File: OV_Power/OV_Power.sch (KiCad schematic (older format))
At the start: 43 parts, among them J4 SpadeLug, J5 SpadeLug, Q1 SSM3K341R, Q2 2N7002BK, U1 LT3796, U2 LT1936

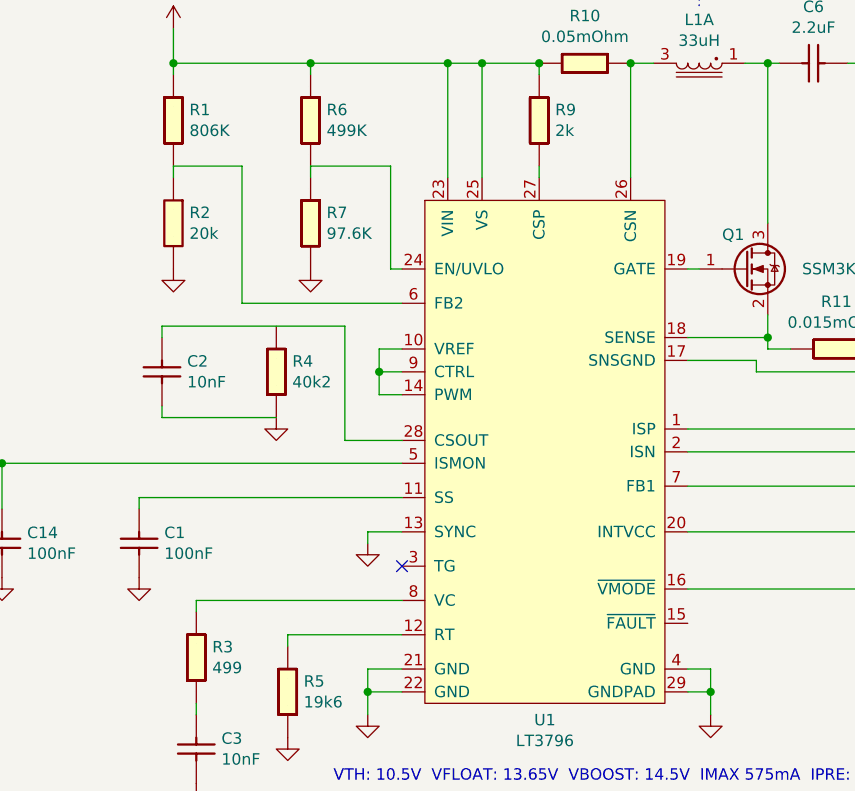
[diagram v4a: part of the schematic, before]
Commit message: Finished schemo and placement of power supply board, then resolved interconnects with the main board.
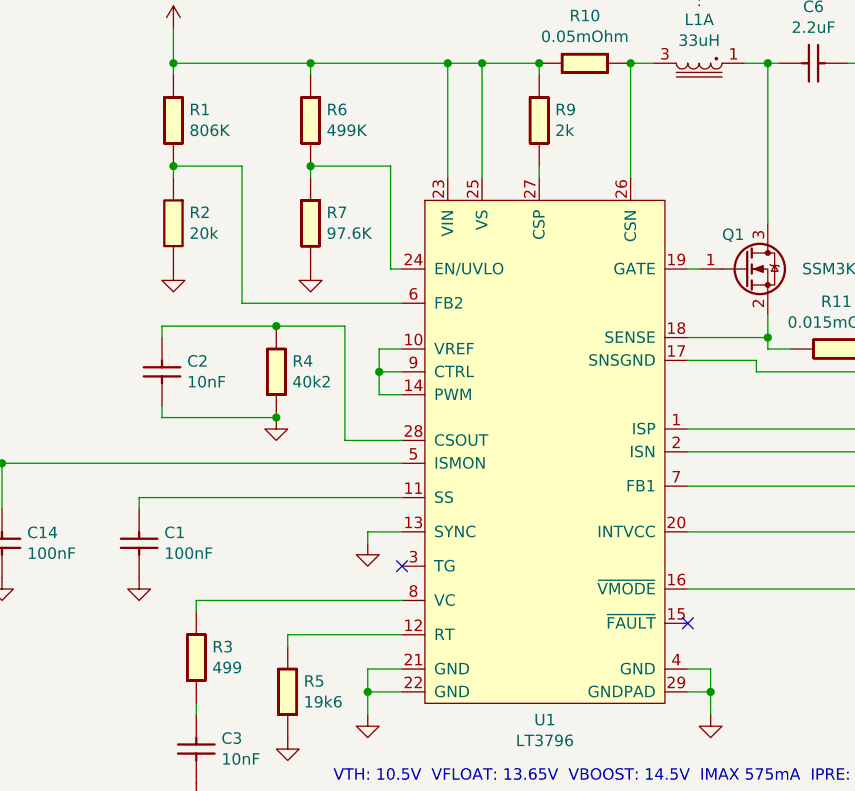
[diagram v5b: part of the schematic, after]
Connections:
- net at C2.1, U1.28 (CSOUT): now also R4.1
- no-connect marks 1 -> 2
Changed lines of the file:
@@
 NoConn ~ 4100 3250
 Wire Wire Line
-	3050 2200 3850 2200
+	3050 2200 3550 2200
 $Sheet
 S 9850 5800 1350 150
@@
 Connection ~ 4700 1050
 Connection ~ 5100 1050
+Connection ~ 3550 2200
+Wire Wire Line
+	3550 2200 3850 2200
+Connection ~ 3550 2600
+Connection ~ 3100 1500
+Connection ~ 3700 1500
+NoConn ~ 5350 3500
 $EndSCHEMATC

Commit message: First cut at complete routing for the power board.  Still need DRC checking and final fettling of the BOM and silkscreens before going to press.
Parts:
- added C15: 100nF_0603_Ceramic_Capacitor,_10%,_X7R,_25V, Capacitor_SMD:C_0603_1608Metric, symbol OpenVent:100nF_0603_Ceramic_Capacitor,_10%,_X7R,_25V
- C5: Tolerance (none) -> 10%; Voltage (none) -> 25V
- D2: Voltage (none) -> 100V
- J4: symbol OV_Power-rescue:SpadeLug-F_connectors -> F_connectors:SpadeLug; Mfr_PN (none) -> 1217861-1
- J5: Mfr_PN (none) -> 1217861-1
- R10, R11, R12, R15: Tolerance (none) -> 1%
- RT1: Tolerance (none) -> 5%
- U1: symbol OV_Power-rescue:LT3796-F_ICs -> F_ICs:LT3796; Desc (none) -> IC LED DRIVER CTRLR DIM 28TSSOP; Detailed (none) -> LED Driver IC 1 Output DC DC Controller SEPIC, Step-Down (B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; Mfr (none) -> Analog Devices; Mfr_PN (none) -> LT3796IFE-1#TRPBF
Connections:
- net GND: now also C15.2
- net VIN_12V: now also C15.1
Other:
- moved on the sheet: R1, R2, R6, R7

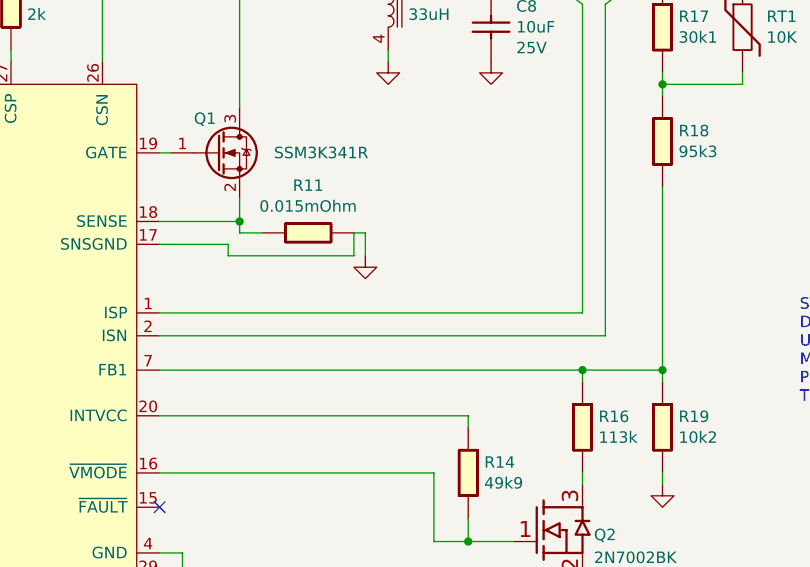
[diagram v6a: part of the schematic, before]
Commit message: Power board routing is finished in 2 layers, but pcb outline is apparently changing yet again...
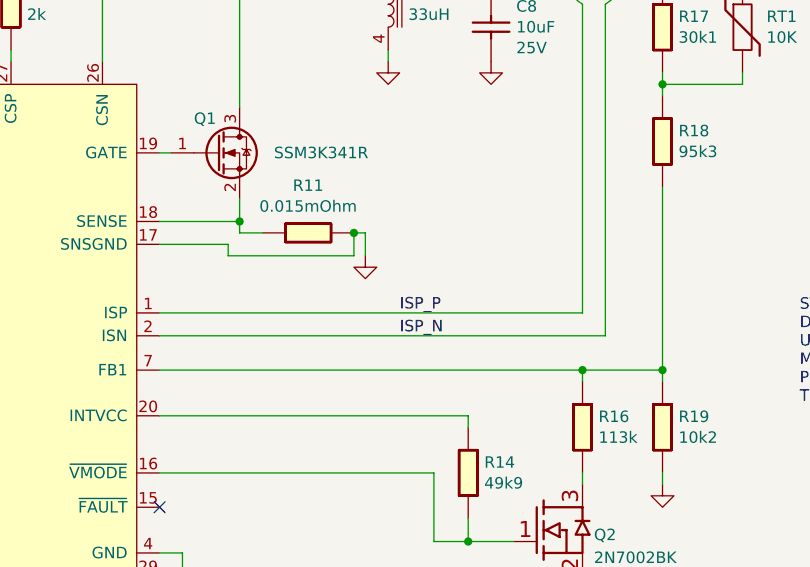
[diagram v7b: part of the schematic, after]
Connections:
- net ISP_P: now reaches C8.1, D3.1 (K), R15.1, U1.1 (ISP)
- net ISP_N: now reaches D4.2 (A), R15.2, R17.1, RT1.1, U1.2 (ISN)
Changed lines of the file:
@@
 Wire Wire Line
 	4300 1150 4300 1050
+Text Label 6400 2650 0    50   ~ 0
+ISP_P
+Text Label 6400 2750 0    50   ~ 0
+ISP_N
+Connection ~ 6200 2300
 $EndSCHEMATC

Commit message: Slight change to schemo per Rick's suggestion, also generated the real BOM.  Gerbers updated, should be ready for production.
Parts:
- J5: symbol OV_Power-rescue:SpadeLug-F_connectors -> OV_Power-rescue:SpadeLug-F_connectors-OV_Power-rescue
- L1: symbol OV_Power-rescue:MSD1260-333-F_inductors -> OV_Power-rescue:MSD1260-333-F_inductors-OV_Power-rescue
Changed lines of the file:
@@
 $EndComp
 $Comp
-L OV_Power-rescue:MSD1260-333-F_inductors L1
+L OV_Power-rescue:MSD1260-333-F_inductors-OV_Power-rescue L1
 U 1 1 5FB0C2C0
 P 5400 1050
@@
 $EndComp
 $Comp
-L OV_Power-rescue:MSD1260-333-F_inductors L1
+L OV_Power-rescue:MSD1260-333-F_inductors-OV_Power-rescue L1
 U 2 1 5FB0D579
 P 6350 1300
@@
 $EndComp
 $Comp
-L OV_Power-rescue:SpadeLug-F_connectors J5
+L OV_Power-rescue:SpadeLug-F_connectors-OV_Power-rescue J5
 U 1 1 5FCBC350
 P 10750 1450
